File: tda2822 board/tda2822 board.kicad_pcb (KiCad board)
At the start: 2 copper layers, 38.6 x 27.8 mm, 14 parts, among them J1 Conn_01x02_Female, J2 Conn_01x02_Female, J3 Conn_01x02_Female, U1 TDA2822

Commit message: Antenna mounts
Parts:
- removed C1: 100u, Capacitor_THT:CP_Radial_D5.0mm_P2.50mm
- U1: moved to B.Cu
- moved U1 8.00 mm to (185.8, 85.0)
- moved C2 5.62 mm to (165.7, 88.4), turned to -90 degrees
- moved C4 3.62 mm to (190.7, 84.1), turned to -90 degrees
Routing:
- net Net-(C2-Pad2): track 16.2 -> 8.53 mm
- net +5V: track 33.1 -> 36.5 mm
- net Net-(C5-Pad1): track 5.64 -> 7.96 mm
- net Net-(C2-Pad1): track 5.45 -> 4.84 mm
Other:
- board size 38.6 x 27.8 mm -> 38.5 x 23.5 mm

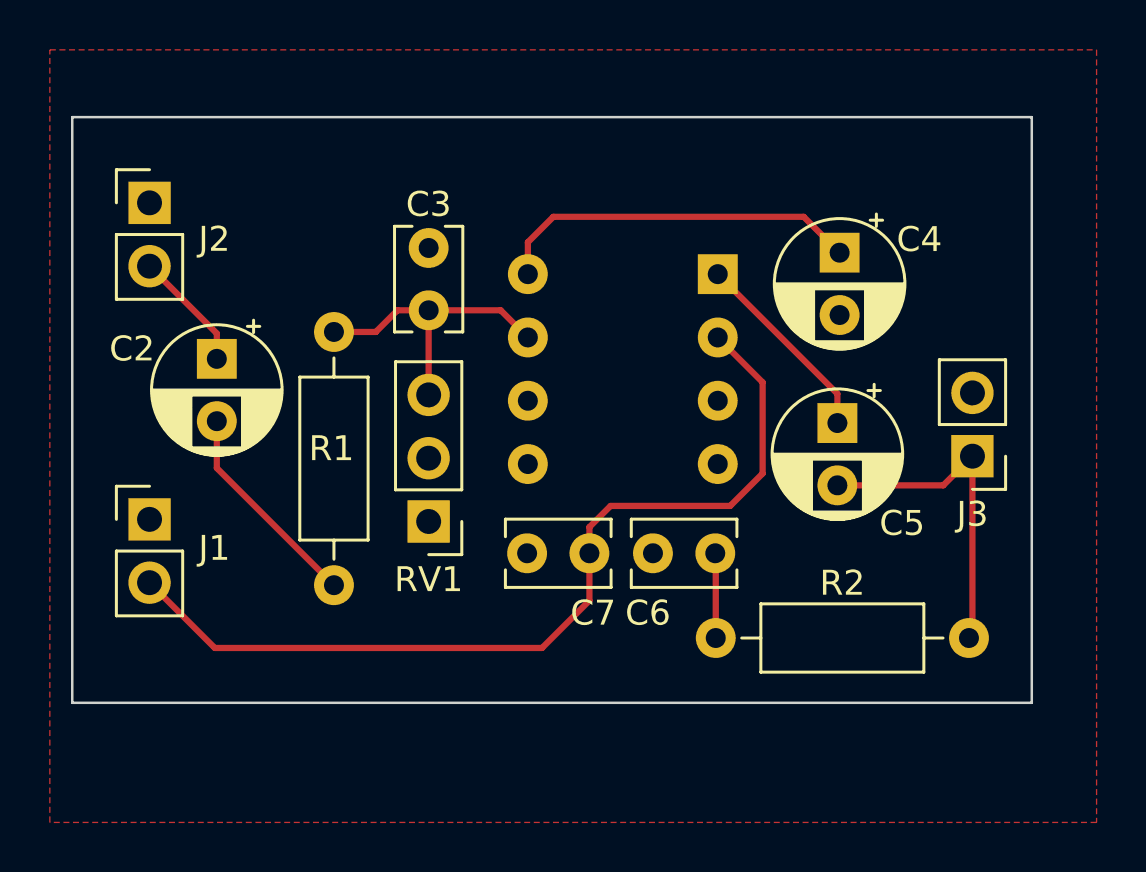
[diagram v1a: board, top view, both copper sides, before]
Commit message: Flip amp board
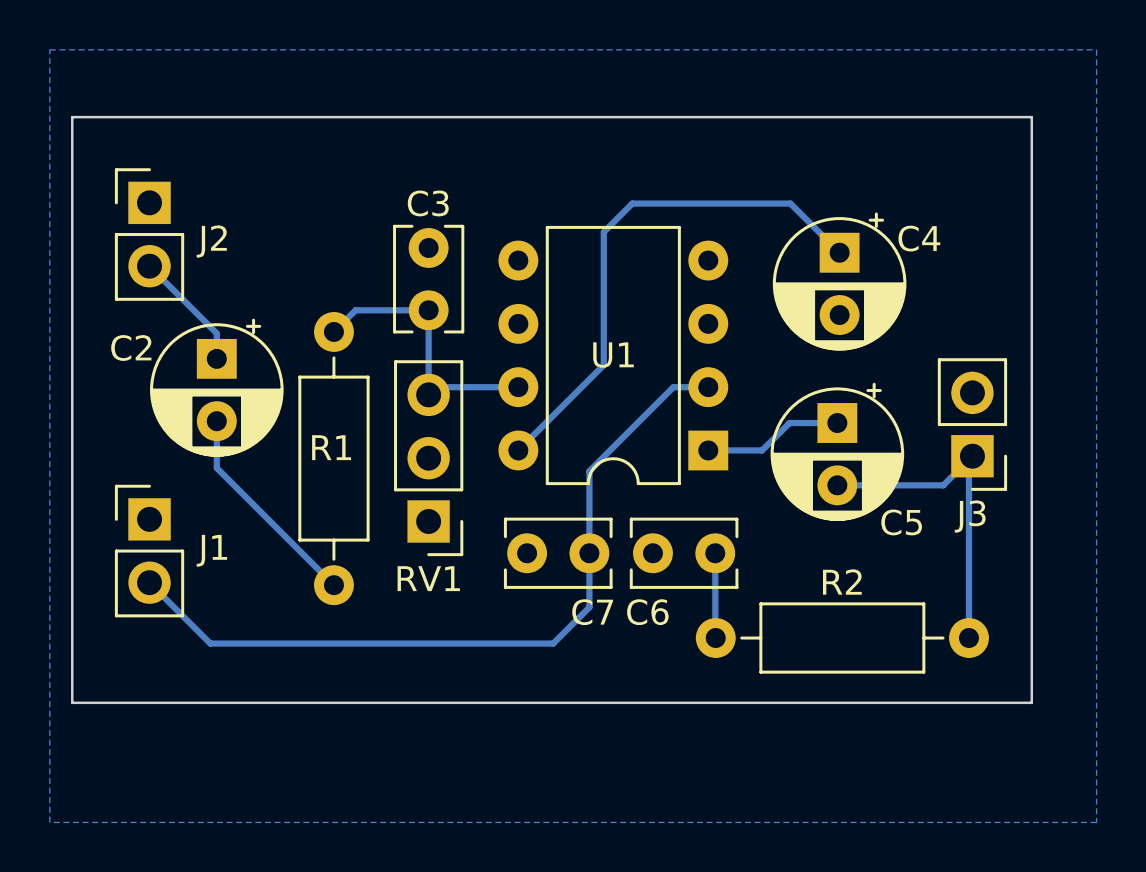
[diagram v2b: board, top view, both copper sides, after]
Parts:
- U1: moved to F.Cu
- moved U1 7.09 mm to (185.4, 92.1)
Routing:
- net Net-(C4-Pad1): track 14.8 -> 20.9 mm
- net +5V: track 36.5 -> 30.9 mm
- net Net-(C5-Pad1): track 7.96 -> 5.64 mm
- net Net-(C3-Pad2): track 12.0 -> 11.3 mm
- added copper zone on B.Cu, net GND
- removed copper zone on F.Cu, net GND
